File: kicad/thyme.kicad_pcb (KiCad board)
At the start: 2 copper layers, 281.8 x 83.1 mm, 90 parts, among them J1 JST BATTERY R, J2 JST BATTERY R, SW1 SW_Push, SW10 SW_Push, SW11 SW_Push, SW12 SW_Push, SW13 SW_Push, SW14 SW_Push, SW15 SW_Push, SW16 SW_Push, SW17 SW_Push, SW18 SW_Push, SW19 SW_Push, SW2 SW_Push, SW20 SW_Push, SW21 SW_Push, SW22 SW_Push, SW23 SW_Push, SW24 SW_Push, SW25 SW_Push, SW26 SW_Push, SW27 SW_Push, SW28 SW_Push, SW29 SW_Push, SW3 SW_Push, SW30 SW_Push, SW31 SW_Push, SW32 SW_Push, SW33 SW_Push, SW34 SW_Push, SW35 SW_Push, SW36 SW_Push, SW37 SW_Push, SW38 SW_Push, SW39 SW_Push, SW4 SW_Push, SW40 SW_Push, SW41 SW_Push, SW42 SW_Push, SW5 SW_Push, SW6 SW_Push, SW7 SW_Push, SW8 SW_Push, SW9 SW_Push, U1 nice_nano, U2 nice_nano

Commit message: chore: move jst to allow room for 1.75u keycaps
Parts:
- moved J1 4.39 mm to (192.0, 98.9)
- moved J2 3.46 mm to (159.3, 98.9)
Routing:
- net RBATTERY_POSITIVE: track 15.9 -> 13.6 mm
- net LBATTERY_POSITIVE: track 9.33 -> 8.26 mm
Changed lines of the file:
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@@
 	(footprint "libraries:CONN_S2B-PH-K-S_JST"
 		(layer "F.Cu")
-		(at 159.30767 102.335499 180)
+		(at 159.30767 98.873099 180)
 		(tags "S2B-PH-K-SLFSN ")
 		(property "Reference" "J2"
@@
 	(footprint "libraries:CONN_S2B-PH-K-S_JST"
 		(layer "F.Cu")
-		(at 192.04767 103.265499 180)
+		(at 192.04767 98.873099 180)
 		(tags "S2B-PH-K-SLFSN ")
 		(property "Reference" "J1"
@@
 		)
 	)
+	(gr_rect
+		(start 225.63257 105.623099)
+		(end 242.63257 130.373099)
+		(stroke
+			(width 0.2)
+			(type default)
+		)
+		(fill no)
+		(layer "B.Cu")
+		(net 79)
+	)
 	(gr_poly
 		(pts
@@
 	)
 	(segment
-		(start 167.38257 99.308099)
-		(end 164.35517 102.335499)
+		(start 159.30767 98.873099)
+		(end 166.94757 98.873099)
 		(width 0.2)
 		(layer "F.Cu")
@@
 	)
 	(segment
-		(start 164.35517 102.335499)
-		(end 159.30767 102.335499)
+		(start 166.94757 98.873099)
+		(end 167.38257 99.308099)
 		(width 0.2)
 		(layer "F.Cu")
@@
 	)
 	(segment
-		(start 192.04767 103.265499)
-		(end 181.41257 92.630399)
+		(start 192.04767 98.873099)
+		(end 184.90267 91.728099)
 		(width 0.2)
 		(layer "B.Cu")
@@
 	)
 	(segment
-		(start 181.41257 92.630399)
+		(start 184.90267 91.728099)
 		(end 181.41257 91.728099)
 		(width 0.2)

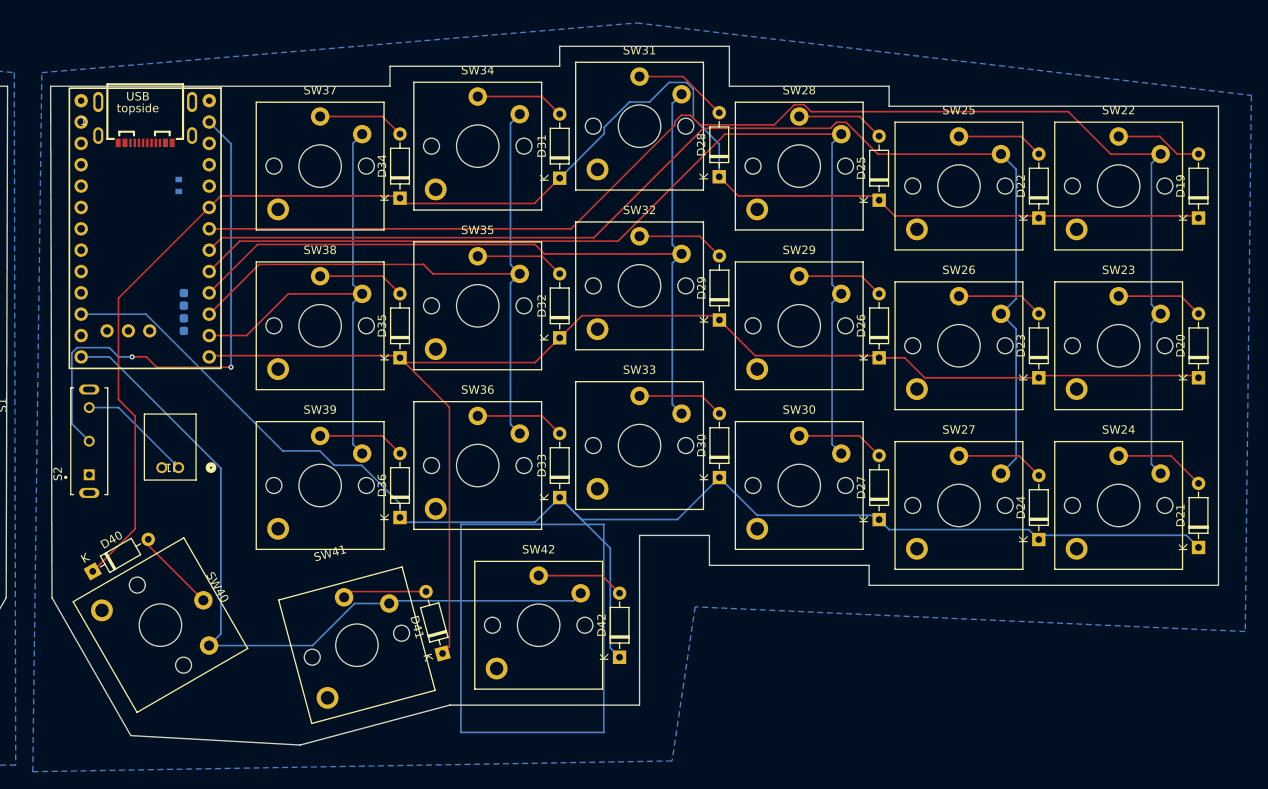
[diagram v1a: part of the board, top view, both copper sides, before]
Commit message: feat: use same cutout for both halves
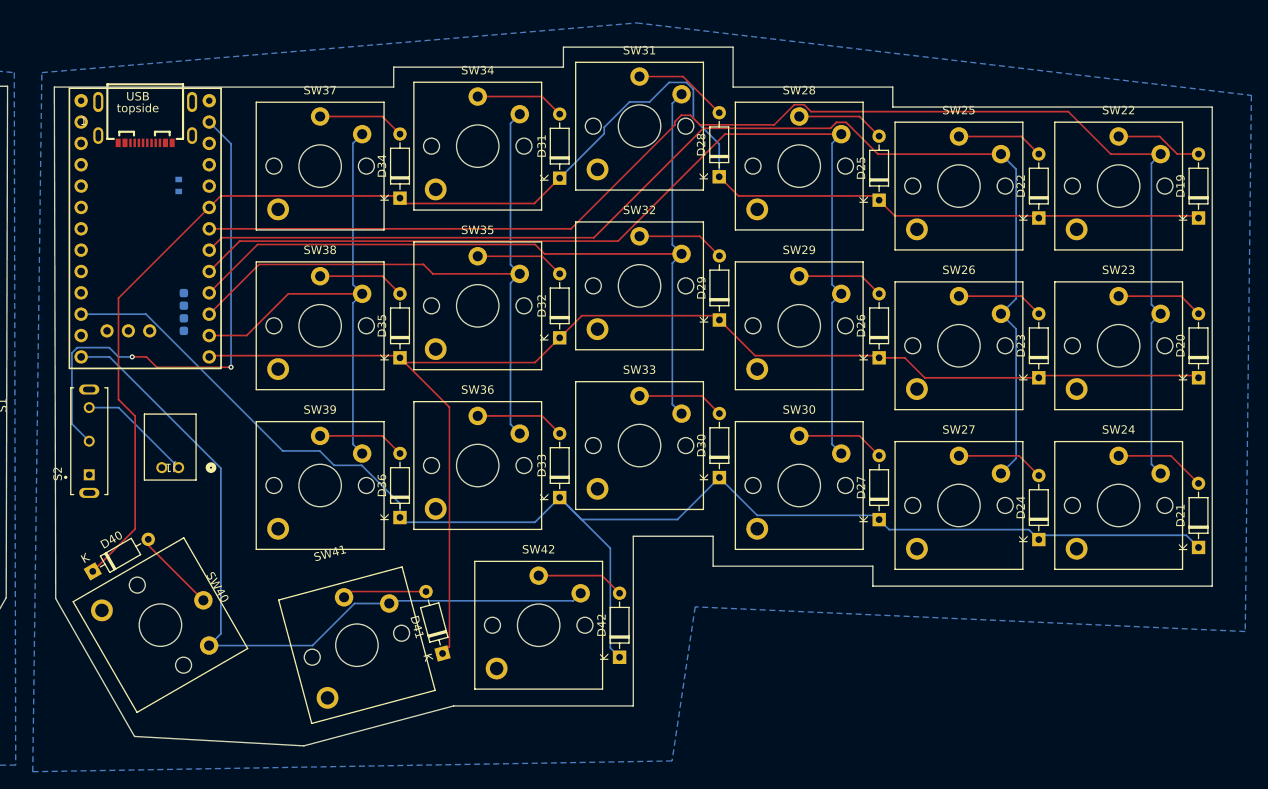
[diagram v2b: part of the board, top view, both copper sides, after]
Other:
- board size 281.8 x 83.1 mm -> 281.1 x 83.2 mm
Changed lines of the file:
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@@
 		)
 	)
-	(gr_rect
-		(start 225.63257 105.623099)
-		(end 242.63257 130.373099)
+	(gr_poly
+		(pts
+			(xy 206.948724 131.973099) (xy 224.761224 127.223099) (xy 246.136224 127.223099) (xy 246.136224 107.035599)
+			(xy 255.636224 107.035599) (xy 255.636224 110.598099) (xy 274.636224 110.598099) (xy 274.636224 112.973099)
+			(xy 315.011224 112.973099) (xy 315.011224 55.973099) (xy 277.011224 55.973099) (xy 277.011224 53.598099)
+			(xy 258.011224 53.598099) (xy 258.011224 48.848099) (xy 237.823724 48.848099) (xy 237.823724 51.223099)
+			(xy 217.636224 51.223099) (xy 217.636224 53.598099) (xy 177.261224 53.598099) (xy 177.425017 114.447237)
+			(xy 186.800159 130.853734)
+		)
 		(stroke
-			(width 0.2)
-			(type default)
+			(width 0.05)
+			(type solid)
 		)
 		(fill no)
-		(layer "B.Cu")
-		(net 79)
+		(layer "Edge.Cuts")
 	)
 	(gr_poly
@@
 		)
 		(stroke
-			(width 0.05)
-			(type solid)
-		)
-		(fill no)
-		(layer "Edge.Cuts")
-	)
-	(gr_poly
-		(pts
-			(xy 206.50757 131.873099) (xy 224.32007 127.123099) (xy 246.88257 127.123099) (xy 246.88257 106.935599)
-			(xy 255.19507 106.935599) (xy 255.19507 110.498099) (xy 274.19507 110.498099) (xy 274.19507 112.873099)
-			(xy 315.75757 112.873099) (xy 315.75757 55.873099) (xy 276.57007 55.873099) (xy 276.57007 53.498099)
-			(xy 257.57007 53.498099) (xy 257.57007 48.748099) (xy 237.38257 48.748099) (xy 237.38257 51.123099)
-			(xy 217.19507 51.123099) (xy 217.19507 53.498099) (xy 176.82007 53.498099) (xy 176.983863 114.347237)
-			(xy 186.359005 130.753734)
-		)
-		(stroke

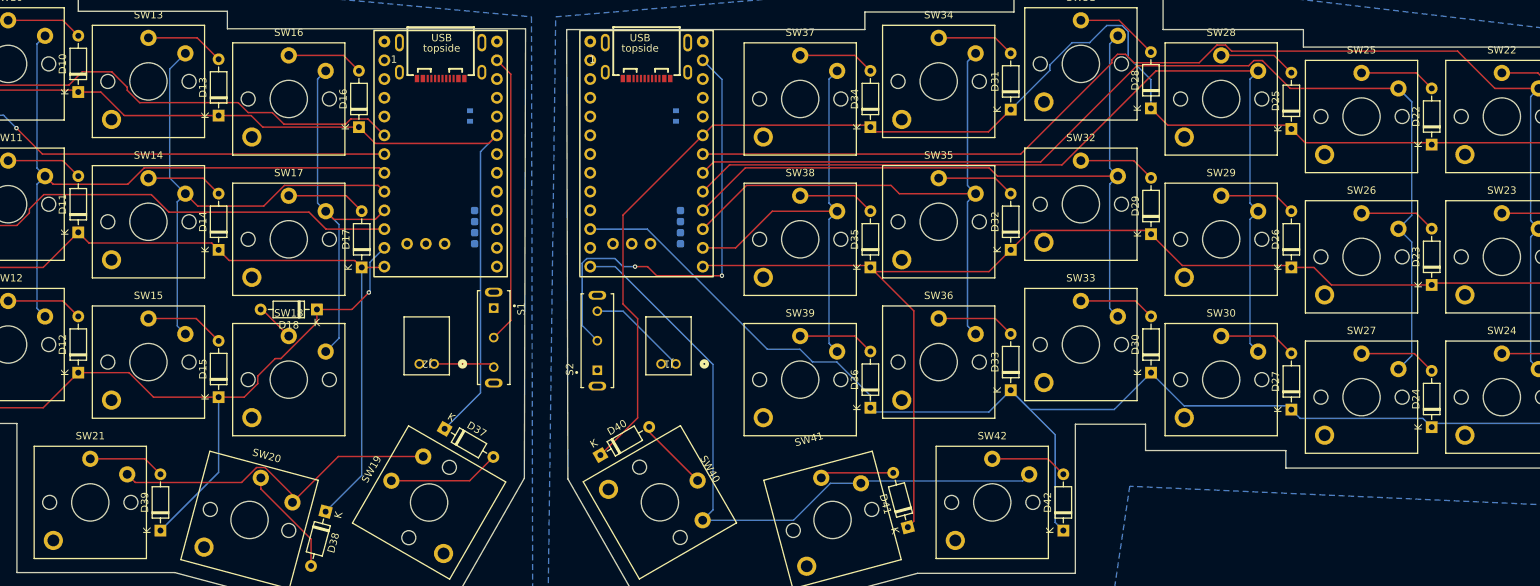
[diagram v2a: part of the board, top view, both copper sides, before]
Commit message: feat: use another row instead of col 7
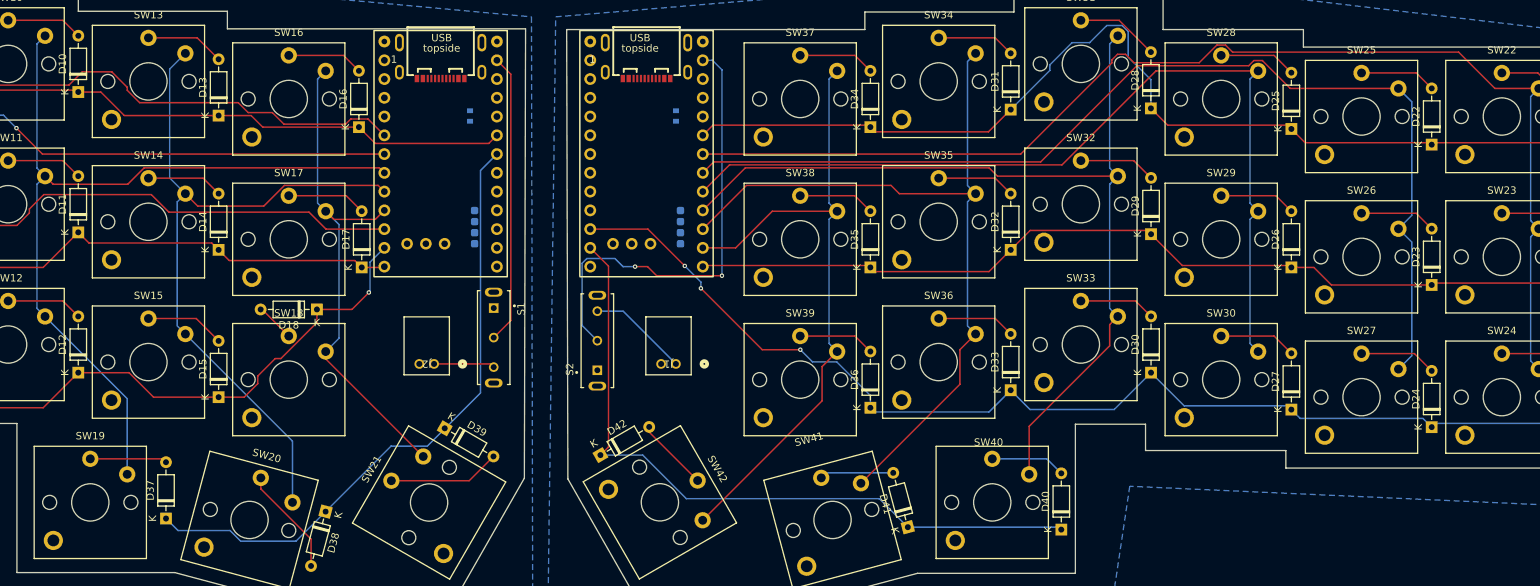
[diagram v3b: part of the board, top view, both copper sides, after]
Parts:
- moved D42 63.5 mm to (181.8, 111.2), turned to 30 degrees
- moved D40 63.2 mm to (244.2, 121.3), turned to 90 degrees
- moved SW19 45.9 mm to (112.8, 117.6), turned to 0 degrees
- moved SW21 45.9 mm to (158.6, 117.6), turned to 60 degrees
- moved SW40 45.0 mm to (234.9, 117.6), turned to 0 degrees
- moved SW42 45.0 mm to (189.9, 117.6), turned to -60 degrees
- moved D39 40.9 mm to (160.7, 107.6), turned to -30 degrees
- moved D37 39.6 mm to (123.0, 119.8), turned to 90 degrees
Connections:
- D37 pad 1: L-ROW0 -> L-ROW3
- D38 pad 1: L-ROW1 -> L-ROW3
- D39 pad 1: L-ROW2 -> L-ROW3
- D40 pad 1: R-ROW0 -> R-ROW3
- D41 pad 1: R-ROW1 -> R-ROW3
- D42 pad 1: R-ROW2 -> R-ROW3
- SW19 pad 2: L-COL6 -> L-COL3
- SW20 pad 2: L-COL6 -> L-COL4
- SW21 pad 2: L-COL6 -> L-COL5
- SW40 pad 2: R-COL6 -> R-COL3
- SW41 pad 2: R-COL6 -> R-COL4
- SW42 pad 2: R-COL6 -> R-COL5
- U1 pad 18: unconnected-(U1-P0.29-LF-Pad18) -> L-ROW3
- U2 pad 11: unconnected-(U2-P1.04-LF-Pad11) -> R-ROW3
- U2 pad 12: R-COL6 -> unconnected-(U2-P1.06-LF-Pad12)
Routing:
- net R-ROW3: track 0.00 -> 96.1 mm
- net R-COL6: track 90.6 -> 0.00 mm
- net L-ROW3: track 0.00 -> 84.6 mm
- net R-ROW0: track 186.9 -> 136.2 mm
- net L-COL6: track 46.5 -> 0.00 mm
- net L-ROW0: track 166.0 -> 123.3 mm
- net R-ROW1: track 161.6 -> 123.7 mm
- net L-ROW1: track 139.2 -> 104.1 mm
- net R-COL5: track 60.1 -> 90.5 mm
- net L-COL4: track 69.8 -> 98.6 mm
- net R-COL4: track 79.7 -> 106.3 mm
- net R-COL3: track 98.9 -> 125.2 mm
- net L-COL3: track 87.4 -> 113.4 mm
- net R-ROW2: track 174.3 -> 153.0 mm, vias 0 -> 3
- net L-ROW2: track 136.9 -> 115.6 mm
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
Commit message: feat: redesign edge cuts and key spacing
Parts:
- SW21, SW42: footprint Switch_Keyboard_Kailh:SW_Kailh_Choc_V1V2_1.00u -> Switch_Keyboard_Kailh:SW_Kailh_Choc_V1V2_1.50u
- moved D41 11.1 mm to (234.6, 121.3)
- moved U2 11.1 mm to (191.6, 55.5)
- moved D19 11.1 mm to (324.5, 69.5)
- moved D20 11.1 mm to (324.5, 88.5)
- moved D21 11.1 mm to (324.5, 108.7)
- moved D22 11.1 mm to (305.5, 69.5)
- moved D23 11.1 mm to (305.5, 88.5)
- moved D24 11.1 mm to (305.5, 107.7)
- moved D25 11.1 mm to (286.5, 67.4)
- moved D26 11.1 mm to (286.5, 86.1)
- moved D27 11.1 mm to (286.5, 105.4)
- moved D28 11.1 mm to (267.5, 64.6)
- moved D29 11.1 mm to (267.5, 81.6)
- moved D30 11.1 mm to (267.5, 100.4)
- moved D31 11.1 mm to (248.5, 64.7)
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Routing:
- net Net-(S2-Pad2): track 62.5 -> 56.9 mm
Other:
- board size 281.1 x 83.2 mm -> 301.5 x 86.3 mm

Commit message: feat: add stabilizers
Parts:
- SW1, SW10, SW11, SW12, SW13, SW14, SW15, SW16, SW17, SW18, SW19, SW2, SW20, SW22, SW23, SW24, SW25, SW26, SW27, SW28, SW29, SW3, SW30, SW31, SW32, SW33, SW34, SW35, SW36, SW37, SW38, SW39, SW4, SW40, SW41, SW5, SW6, SW7, SW8, SW9: footprint Switch_Keyboard_Kailh:SW_Kailh_Choc_V1V2_1.00u -> PCM_Switch_Keyboard_Hotswap_Kailh:SW_Hotswap_Kailh_Choc_V1V2_1.00u
- SW21, SW42: footprint Switch_Keyboard_Kailh:SW_Kailh_Choc_V1V2_1.50u -> PCM_Switch_Keyboard_Hotswap_Kailh:SW_Hotswap_Kailh_Choc_V1V2_1.00u
- moved D37 5.40 mm to (115.3, 125.1)
- moved D1 4.02 mm to (46.4, 72.6)
- moved D12 3.77 mm to (103.4, 103.7)
- moved D9 3.77 mm to (84.4, 108.4)
- moved D22 3.64 mm to (305.3, 73.1)
- moved D38 3.59 mm to (136.0, 122.2)
- moved D11 3.56 mm to (103.4, 84.5)
- moved D4 3.56 mm to (65.4, 72.6)
- moved D41 3.56 mm to (235.3, 124.8)
- moved D26 3.55 mm to (286.5, 89.7)
- moved D23 3.49 mm to (305.5, 92.0)
- moved D19 3.46 mm to (324.5, 72.9)
- moved D35 3.43 mm to (229.3, 89.5)
- moved D36 3.42 mm to (229.3, 108.5)
- moved D20 3.42 mm to (324.5, 91.9)
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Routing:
- net R-COL3: track 125.2 -> 144.9 mm, vias 0 -> 2
- net R-COL4: track 106.3 -> 124.3 mm, vias 0 -> 1
- net R-COL5: track 90.5 -> 104.1 mm, vias 0 -> 1
- net R-ROW0: track 136.2 -> 124.2 mm
- net R-COL2: track 121.8 -> 133.8 mm, vias 0 -> 1
- net R-COL0: track 162.8 -> 172.5 mm, vias 0 -> 1
- net L-ROW3: track 84.6 -> 92.9 mm
- net L-COL0: track 150.5 -> 142.7 mm
- net L-COL1: track 128.6 -> 121.1 mm, vias 2 -> 1
- net L-COL5: track 69.0 -> 62.4 mm
- net Net-(D37-A): track 10.4 -> 16.2 mm
- net Net-(D38-A): track 14.7 -> 20.2 mm
- net L-COL4: track 98.6 -> 93.2 mm, vias 0 -> 1
- net Net-(D1-A): track 10.2 -> 15.4 mm
- net Net-(D9-A): track 10.4 -> 15.5 mm
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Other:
- board size 301.5 x 86.3 mm -> 301.4 x 86.3 mm

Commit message: feat: move to 6 connectors and remove silkscreen lables
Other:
- board text added: "topside"
